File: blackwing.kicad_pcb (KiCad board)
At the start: 2 copper layers, 136.5 x 121.3 mm, 36 parts, among them J1 Conn_01x04, SW00 SW_Push, SW01 SW_Push, SW02 SW_Push, SW03 SW_Push, SW04 SW_Push, SW05 SW_Push, SW10 SW_Push, SW11 SW_Push, SW12 SW_Push, SW13 SW_Push, SW14 SW_Push, SW15 SW_Push, SW20 SW_Push, SW21 SW_Push, SW22 SW_Push, SW23 SW_Push, SW24 SW_Push, SW25 SW_Push, SW30 SW_Push, SW31 SW_Push, SW32 SW_Push, SW33 SW_Push, SW34 SW_Push, SW35 SW_Push, SW40 SW_Push, SW41 SW_Push, SW42 SW_Push, SW43 SW_Push, SW44 SW_Push, SW45 SW_Push, SW50 SW_Push, U1 CORE51822, U2 CORE51822

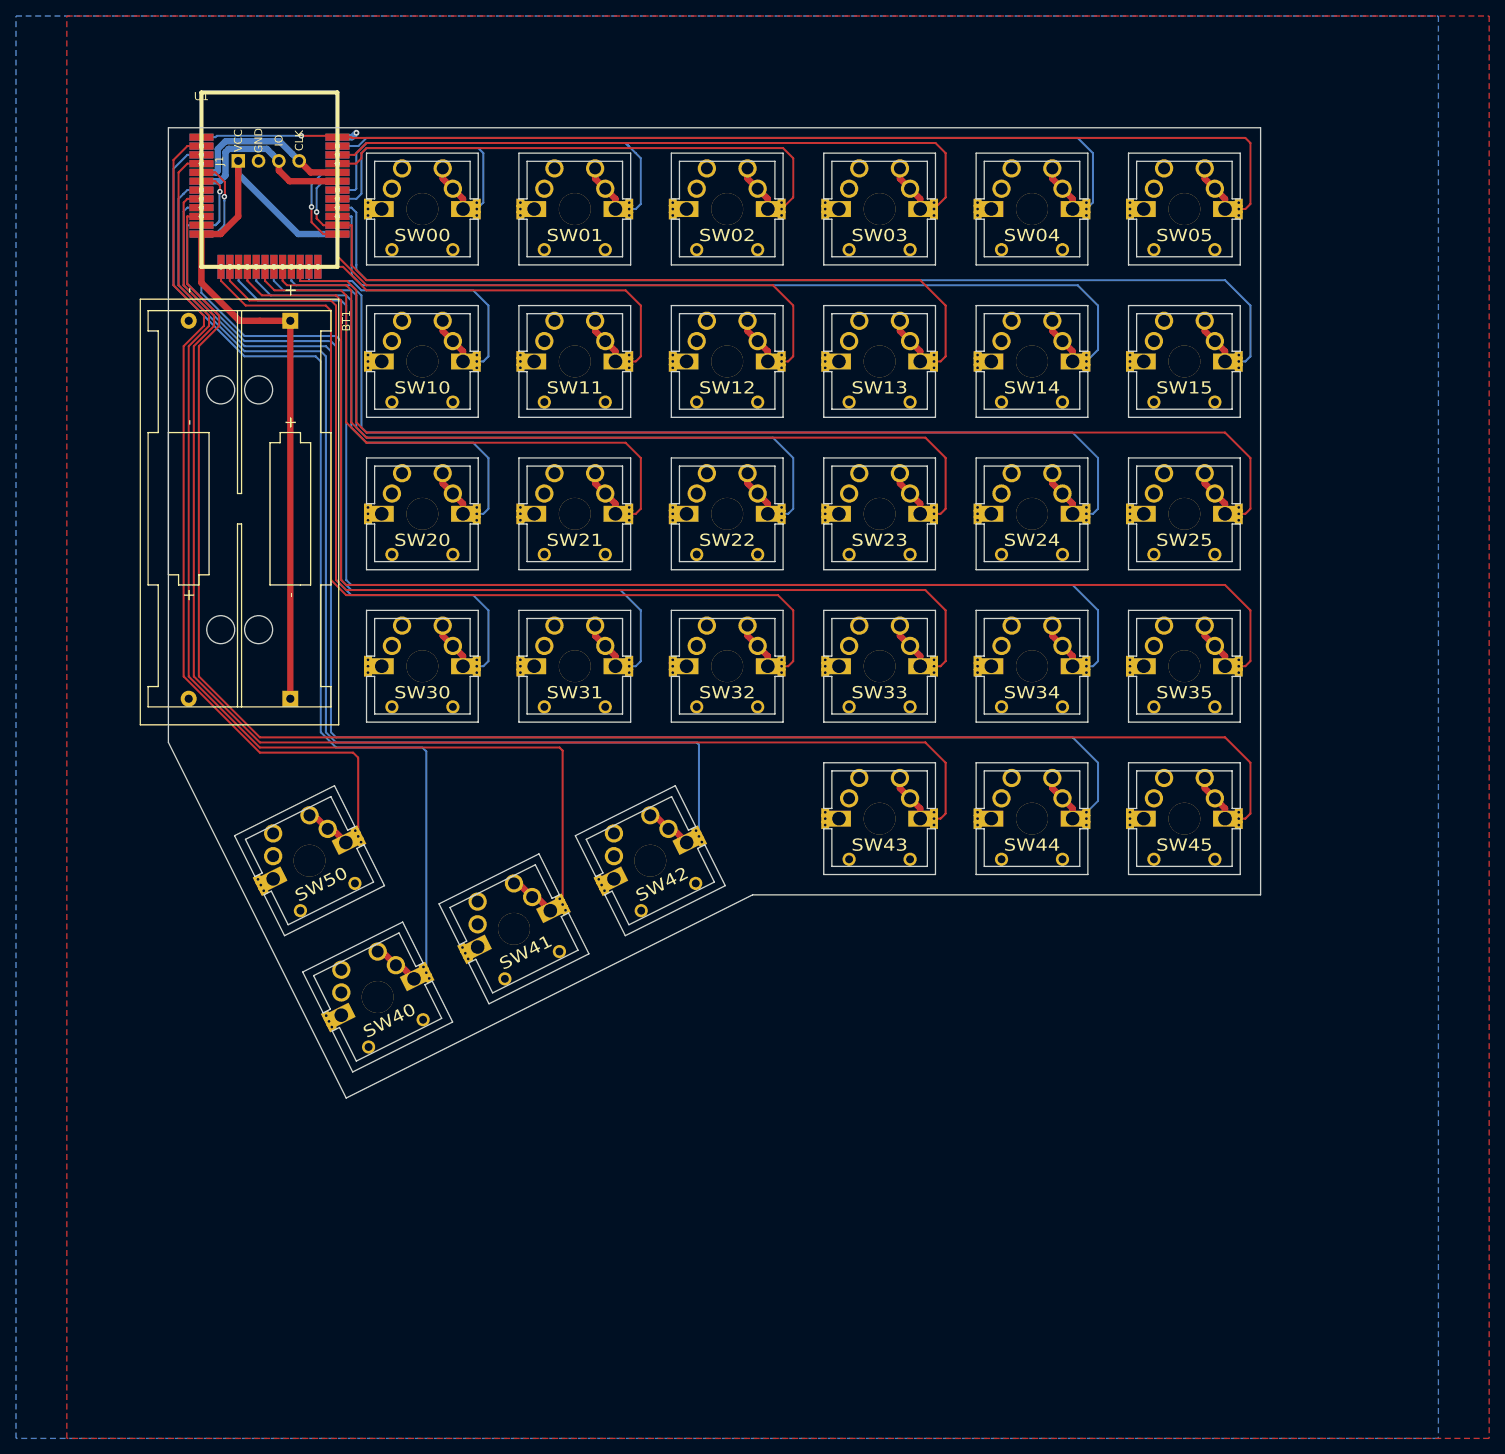
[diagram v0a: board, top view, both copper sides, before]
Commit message: vertically staggered design
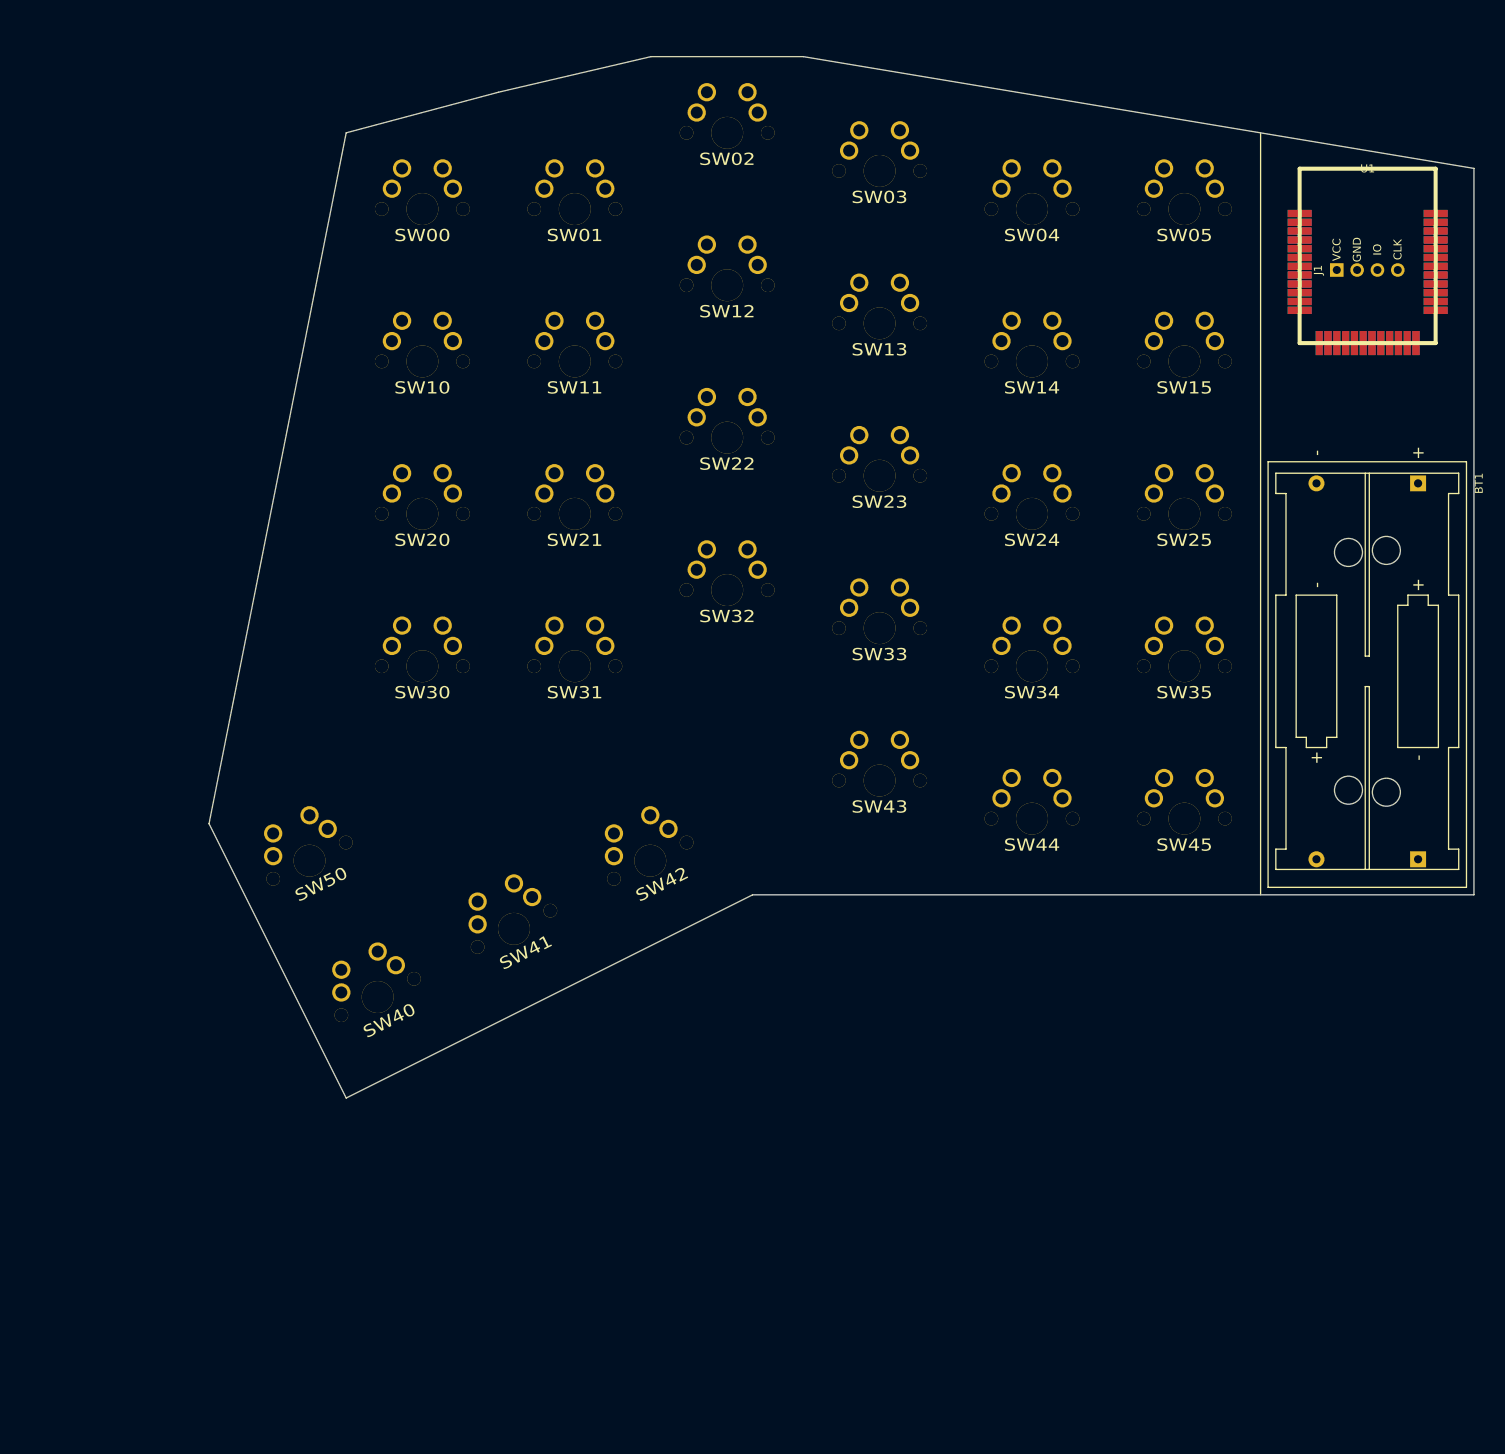
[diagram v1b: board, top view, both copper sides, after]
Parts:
- SW00, SW01, SW02, SW03, SW04, SW05, SW10, SW11, SW12, SW13, SW14, SW15, SW20, SW21, SW22, SW23, SW24, SW25, SW30, SW31, SW32, SW33, SW34, SW35, SW40, SW41, SW42, SW43, SW44, SW45, SW50: footprint blackwing:MX_FLIP_CUTOUT -> blackwing:MX_FLIP_5Pin
- moved U1 146.1 mm to (149.9, 5.12)
- moved BT1 142.4 mm to (156.2, 44.5)
- moved BT2 142.4 mm to (156.2, 91.4)
- moved J1 138.0 mm to (146.1, 17.8)
- moved U2 129.1 mm to (149.9, 5.12)
- moved SW32 9.53 mm to (69.8, 57.8)
- moved SW12 9.53 mm to (69.8, 19.7)
- moved SW02 9.53 mm to (69.8, 0.64)
- moved SW22 9.52 mm to (69.8, 38.7)
- moved SW33 4.76 mm to (88.9, 62.5)
- moved SW43 4.76 mm to (88.9, 81.6)
- moved SW03 4.76 mm to (88.9, 5.40)
- moved SW13 4.76 mm to (88.9, 24.4)
- moved SW23 4.76 mm to (88.9, 43.5)
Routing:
- net S45: track 215.4 -> 0.00 mm, vias 1 -> 0
- net S44: track 195.6 -> 0.00 mm, vias 1 -> 0
- net S35: track 182.2 -> 0.00 mm, vias 1 -> 0
- net S43: track 180.2 -> 0.00 mm, vias 1 -> 0
- net S34: track 163.8 -> 0.00 mm, vias 1 -> 0
- net S25: track 156.9 -> 0.00 mm, vias 1 -> 0
- net S42: track 151.5 -> 0.00 mm, vias 1 -> 0
- net S05: track 150.4 -> 0.00 mm, vias 1 -> 0
- net S41: track 148.3 -> 0.00 mm, vias 1 -> 0
- net S33: track 145.9 -> 0.00 mm, vias 1 -> 0
- net S15: track 140.9 -> 0.00 mm, vias 1 -> 0
- net S24: track 138.9 -> 0.00 mm, vias 1 -> 0
- net S40: track 138.9 -> 0.00 mm, vias 1 -> 0
- net S32: track 127.6 -> 0.00 mm, vias 1 -> 0
- net S31: track 125.9 -> 0.00 mm, vias 1 -> 0
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- removed copper zone on B.Cu, net GND
- removed copper zone on F.Cu, net GND
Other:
- board size 136.5 x 121.3 mm -> 158.1 x 130.2 mm

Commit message: version 2
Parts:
- J1, U1: moved to B.Cu
- SW00, SW01, SW02, SW03, SW04, SW05, SW10, SW11, SW12, SW13, SW14, SW15, SW20, SW21, SW22, SW23, SW24, SW25, SW30, SW31, SW32, SW33, SW34, SW35, SW40, SW41, SW42, SW43, SW44, SW45, SW50: footprint blackwing:MX_FLIP_5Pin -> blackwing:MX_FLIP
- U2: moved to F.Cu
- moved U2 28.2 mm to (164.9, 28.9), turned to 270 degrees
- moved U1 28.2 mm to (164.9, 28.9), turned to 90 degrees
- moved SW40 13.8 mm to (12.7, 105.4), turned to 0 degrees
- moved SW41 12.2 mm to (31.8, 95.9), turned to 0 degrees
- moved J1 11.2 mm to (147.3, 28.9), turned to 270 degrees
- moved SW43 9.53 mm to (88.9, 91.1)
- moved SW42 9.45 mm to (50.8, 91.1), turned to 0 degrees
- moved SW50 7.21 mm to (12.7, 86.4), turned to 0 degrees
- moved SW01 7.14 mm to (50.8, 3.02)
- moved SW24 4.76 mm to (108.0, 53.0)
- moved SW25 4.76 mm to (127.0, 53.0)
- moved SW30 4.76 mm to (31.8, 62.5)
- moved SW34 4.76 mm to (108.0, 72.1)
- moved SW35 4.76 mm to (127.0, 72.1)
- moved SW44 4.76 mm to (108.0, 91.1)
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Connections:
- U1 pad 10: S45 -> S35
- U1 pad 13: S32 -> S33
- U1 pad 14: S33 -> S32
- U1 pad 15: S34 -> S30
- U1 pad 16: S35 -> S25
- U1 pad 17: S20 -> S24
- U1 pad 19: S22 -> S23
- U1 pad 2: S50 -> S44
- U1 pad 20: S23 -> S22
- U1 pad 21: S24 -> S20
- U1 pad 22: S25 -> S15
- U1 pad 23: S10 -> S14
- U1 pad 25: S12 -> S01
- U1 pad 26: S13 -> S04
- U1 pad 27: S14 -> S13
- U1 pad 28: S15 -> S12
- U1 pad 29: S00 -> S10
- U1 pad 3: S40 -> S43
- U1 pad 30: S01 -> S05
- U1 pad 33: S02 -> S03
- U1 pad 34: S03 -> S02
- U1 pad 35: S04 -> S00
- U1 pad 36: S05 -> S45
- U1 pad 4: S41 -> S42
- U1 pad 6: S30 -> S34
- U1 pad 7: S42 -> S41
- U1 pad 8: S43 -> S40
- U1 pad 9: S44 -> S50
- U2 pad 10: S14 -> S13
- U2 pad 14: S10 -> S14
- U2 pad 15: S25 -> S15
- U2 pad 16: S24 -> S20
- U2 pad 17: S23 -> S22
- U2 pad 18: S22 -> S23
- U2 pad 2: S04 -> S00
- U2 pad 20: S20 -> S24
- U2 pad 21: S35 -> S25
- U2 pad 22: S34 -> S30
- U2 pad 23: S33 -> S32
- U2 pad 24: S32 -> S33
- U2 pad 26: S30 -> S34
- U2 pad 27: S45 -> S35
- U2 pad 28: S44 -> S50
- U2 pad 29: S43 -> S40
- U2 pad 3: S03 -> S02
- U2 pad 30: S42 -> S41
- U2 pad 33: S41 -> S42
- U2 pad 34: S40 -> S43
- U2 pad 35: S50 -> S44
- U2 pad 36: S05 -> S45
- U2 pad 4: S02 -> S03
- U2 pad 5: S12 -> S01
- U2 pad 6: S13 -> S04
- U2 pad 7: S01 -> S05
- U2 pad 8: S00 -> S10
- U2 pad 9: S15 -> S12
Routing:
- net S40: track 0.00 -> 179.0 mm, vias 0 -> 1
- net S50: track 0.00 -> 170.0 mm, vias 0 -> 1
- net S41: track 0.00 -> 156.6 mm, vias 0 -> 1
- net S00: track 0.00 -> 141.6 mm, vias 0 -> 1
- net S42: track 0.00 -> 140.2 mm, vias 0 -> 1
- net S30: track 0.00 -> 136.7 mm, vias 0 -> 1
- net S10: track 0.00 -> 132.0 mm, vias 0 -> 1
- net S01: track 0.00 -> 129.5 mm, vias 0 -> 1
- net S20: track 0.00 -> 127.8 mm, vias 0 -> 1
- net S31: track 0.00 -> 122.1 mm, vias 0 -> 1
- net S43: track 0.00 -> 101.5 mm, vias 0 -> 1
- net S21: track 0.00 -> 101.5 mm, vias 0 -> 1
- net S02: track 0.00 -> 99.2 mm, vias 0 -> 1
- net S11: track 0.00 -> 93.8 mm, vias 0 -> 1
- net S32: track 0.00 -> 92.4 mm, vias 0 -> 1
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- added copper zone on B.Cu, net GND
- added copper zone on F.Cu, net GND
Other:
- board size 158.1 x 130.2 mm -> 161.9 x 123.8 mm
- net class Default: clearance 0.1524 -> 0.254; trace_width 0.1524 -> 0.254
- rule trace_clearance: 0.1524 -> 0.254
